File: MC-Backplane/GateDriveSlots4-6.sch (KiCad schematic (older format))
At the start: 3 parts, among them U16 86094328314755V1LF, U17 86094328314755V1LF, U18 86094328314755V1LF

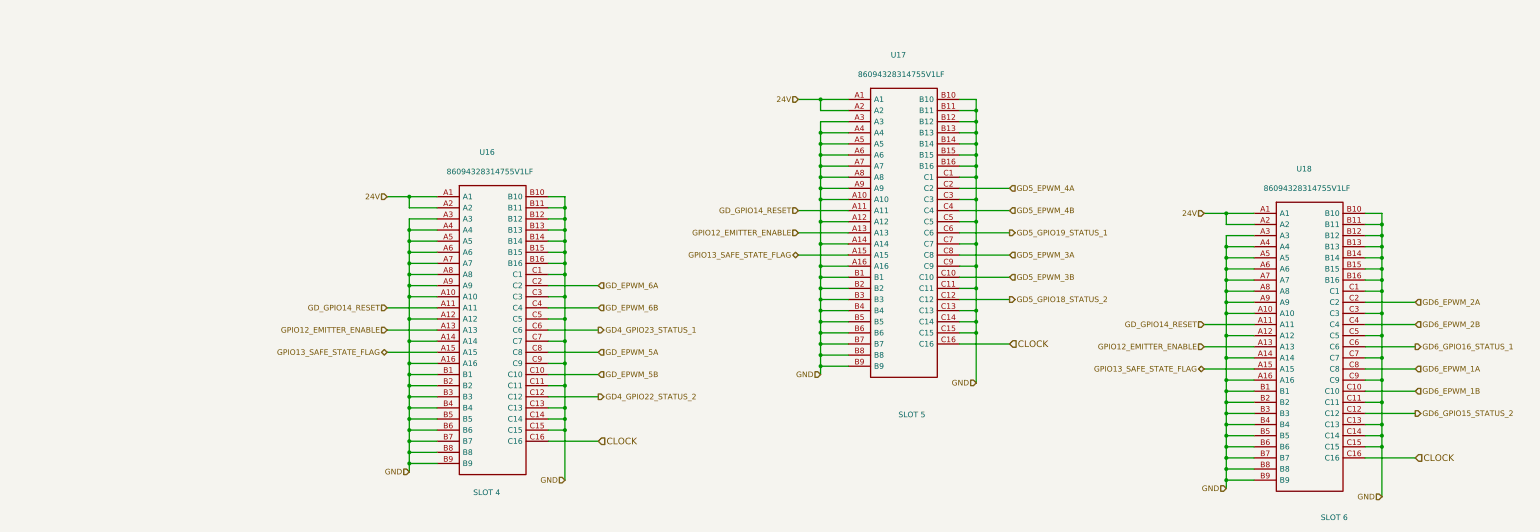
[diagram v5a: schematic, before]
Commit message: schematic reorg and layout begins
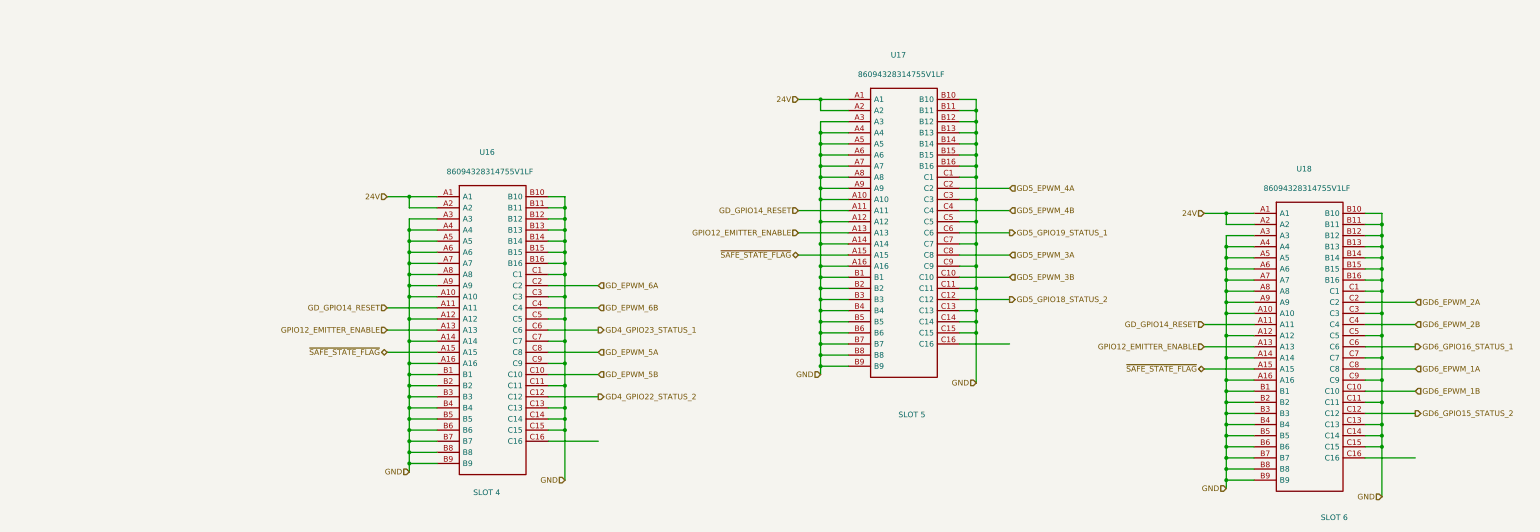
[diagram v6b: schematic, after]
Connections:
- net CLOCK: no longer names the net of U16.C16, U17.C16, U18.C16
- net GPIO13_SAFE_STATE_FLAG renamed ~SAFE_STATE_FLAG~
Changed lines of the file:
@@
 $Descr A4 11693 8268
 encoding utf-8
-Sheet 5 7
+Sheet 5 19
 Title ""
 Date ""
@@
 GPIO12_EMITTER_ENABLE
 Text HLabel 1300 4300 0    50   BiDi ~ 0
-GPIO13_SAFE_STATE_FLAG
+~SAFE_STATE_FLAG~
 Text HLabel 5000 3025 0    50   Input ~ 0
 GD_GPIO14_RESET
@@
 GPIO12_EMITTER_ENABLE
 Text HLabel 5000 3425 0    50   BiDi ~ 0
-GPIO13_SAFE_STATE_FLAG
+~SAFE_STATE_FLAG~
 Text HLabel 8650 4050 0    50   Input ~ 0
 GD_GPIO14_RESET
@@
 GPIO12_EMITTER_ENABLE
 Text HLabel 8650 4450 0    50   BiDi ~ 0
-GPIO13_SAFE_STATE_FLAG
+~SAFE_STATE_FLAG~
 Text HLabel 3200 5100 2    59   Input ~ 0
-CLOCK
 Text HLabel 6900 4225 2    59   Input ~ 0
-CLOCK
 Text HLabel 10550 5250 2    59   Input ~ 0
-CLOCK
 Text HLabel 3200 4300 2    50   Input ~ 0
 GD_EPWM_5A
